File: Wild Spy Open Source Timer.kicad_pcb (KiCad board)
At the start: 2 copper layers, 30 x 32.8 mm, 74 parts, among them Q1 AO3415, Q2 AO3415, Q3 AO3415, Q4 AO3415, Q5 AO3415, Q6 AO3415, SW1 SW_PUSH, SW2 ORD213, U1 DS3232SN, U2 TPS70933DBVR, U3 UM6K33N, U4 UM6K33N, U5 ATSAMD21E16B

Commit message: Generated Gerbers for Rev1 Generated BOM for Rev1 Generated renders for Rev1 Some updating of paths and libs
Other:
- net class Default: clearance 0.2032 -> 0.1524; trace_width 0.2032 -> 0.1524
- rule trace_clearance: 0.2032 -> 0.1524

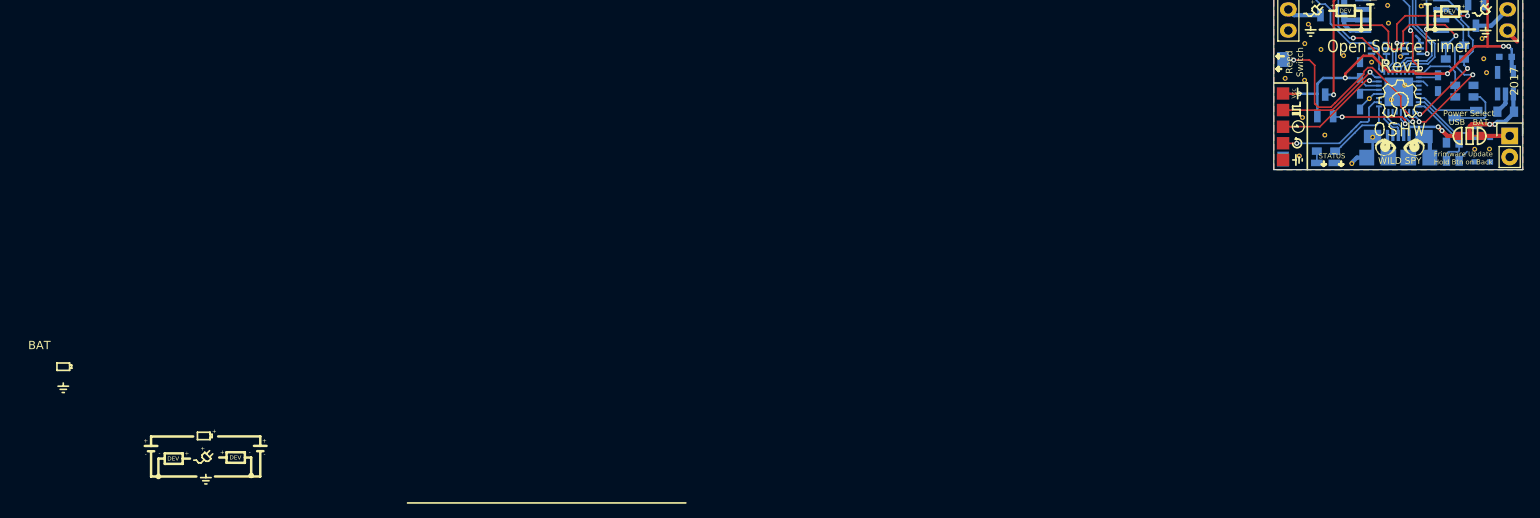
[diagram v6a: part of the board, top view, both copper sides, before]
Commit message: Fixed bug in library - wrong 3d model for USB Fixed Front layer silkscreen - had no battery reference of voltage range Regenerated Gerbers Regenerated renders
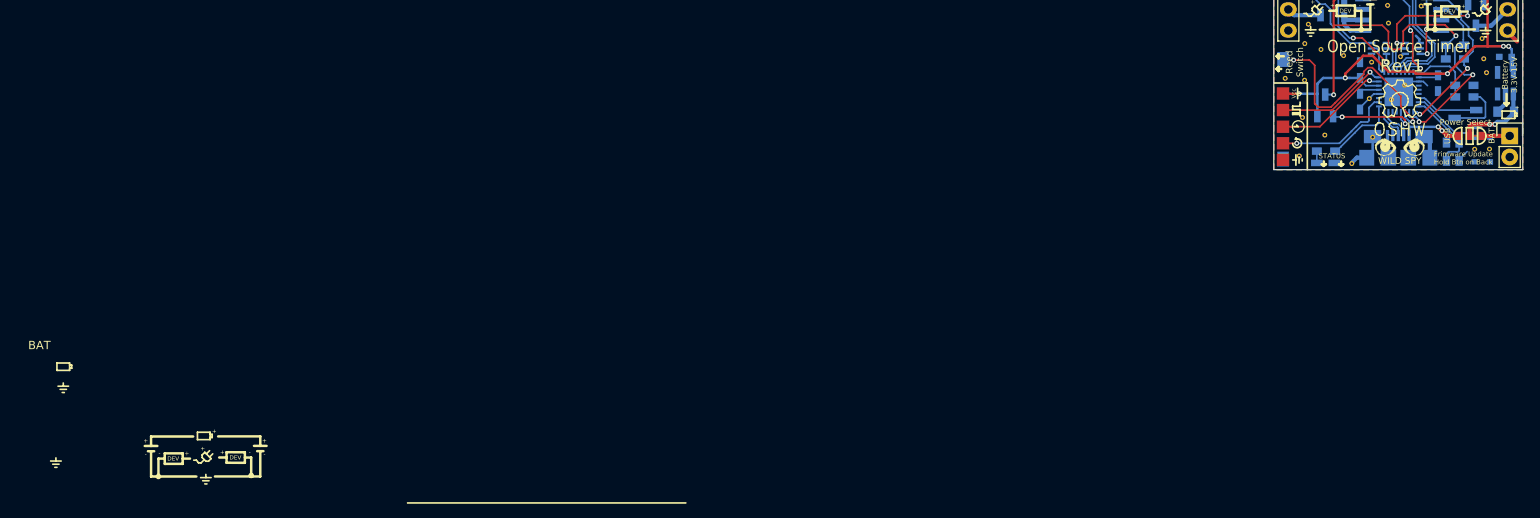
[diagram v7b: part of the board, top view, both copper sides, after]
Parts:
- R10: value 3.3k -> 2k
- R9: value 1.7k -> 1k
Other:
- board text added: "Battery 3.3V-15V"
- board text removed: "USB BAT"

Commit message: Removed Harry's commit of WavTriggerBoard.  Should not be in this repo. Updated chip in schematic.
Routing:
- net (no net): track 0.00 -> 51.9 mm
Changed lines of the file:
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@@
   (general
     (links 148)
-    (no_connects 11)
-    (area 181.559 88.4322 228.9558 130.681609)
+    (no_connects 1)
+    (area 188.924999 94.158999 219.075001 127.075001)
     (thickness 1.6)
     (drawings 501)
-    (tracks 448)
+    (tracks 451)
     (zones 0)
     (modules 74)
@@
     (effects (font (size 0.8 0.8) (thickness 0.2)))
   )
+  (segment (start 238.5568 86.9061) (end 238.5568 107.2134) (width 0.1524) (layer Dwgs.User) (net 0))
+  (segment (start 207.4672 76.2635) (end 224.7646 93.5609) (width 0.1524) (layer Dwgs.User) (net 0))
+  (segment (start 200.3171 76.2635) (end 207.4672 76.2635) (width 0.1524) (layer Dwgs.User) (net 0))
   (segment (start 215.011 121.539) (end 213.578 121.539) (width 0.2032) (layer B.Cu) (net 1))
   (segment (start 213.578 121.539) (end 213.39 121.727) (width 0.2032) (layer B.Cu) (net 1))
